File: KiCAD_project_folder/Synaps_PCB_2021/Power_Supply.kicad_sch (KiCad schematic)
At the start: 7 parts, among them J1 USB_C_Receptacle, U1 MAX14748BEWW+

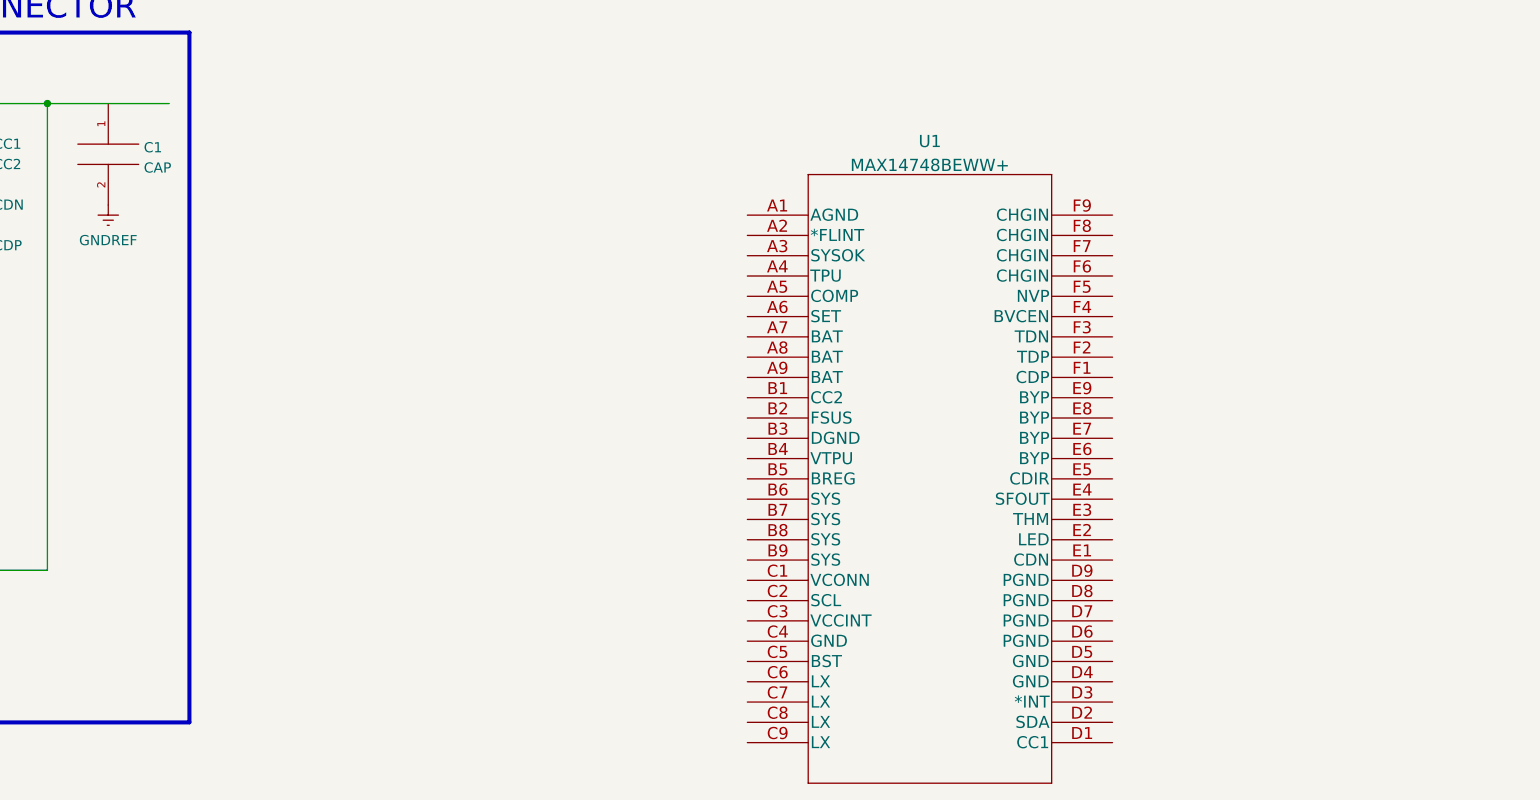
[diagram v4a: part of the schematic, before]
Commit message: modified the battery file
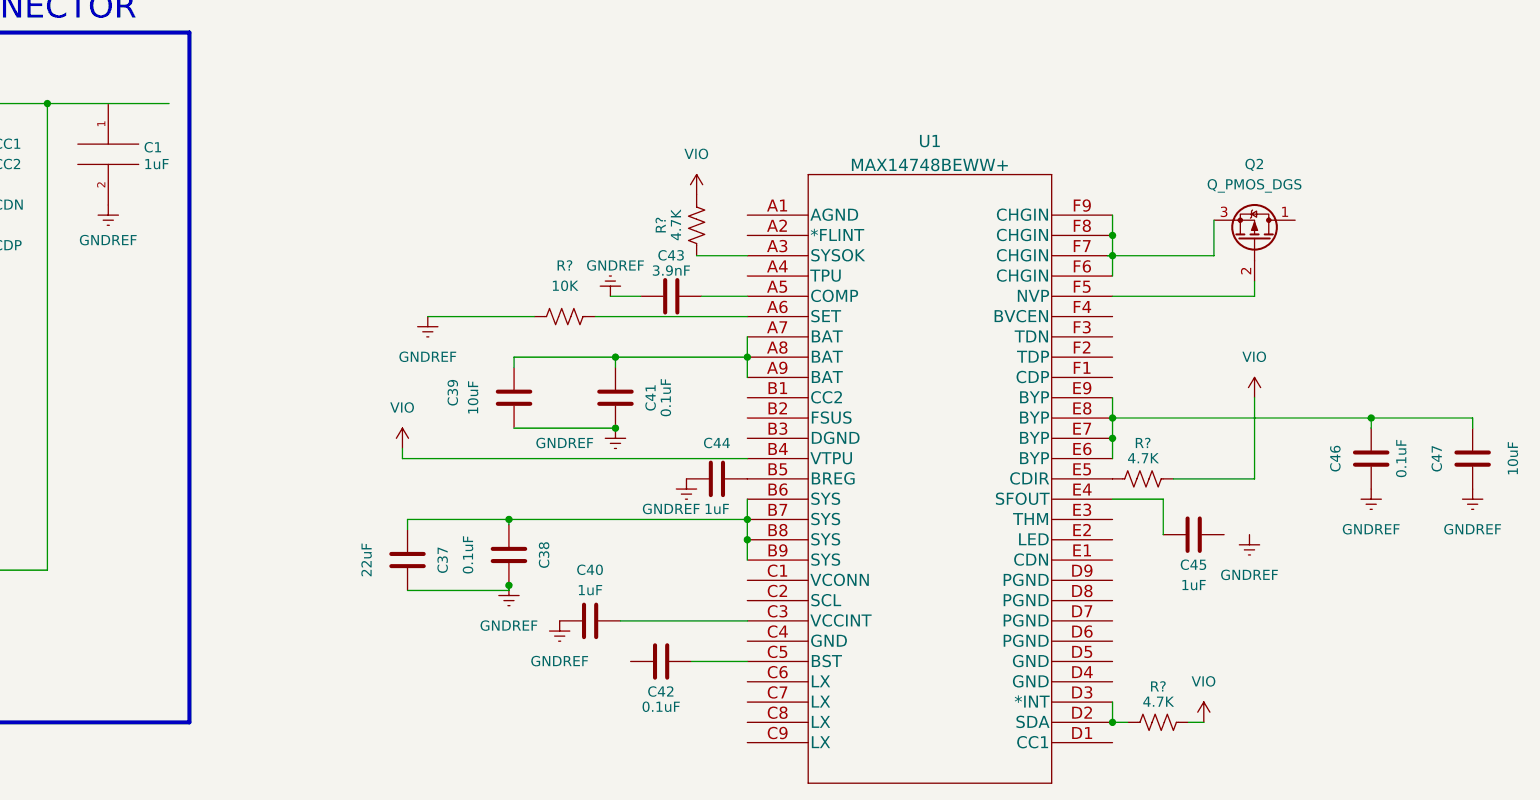
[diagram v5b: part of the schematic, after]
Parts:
- added C37: 22uF, symbol Device:C
- added C38, C41, C42, C46: 0.1uF, symbol Device:C
- added C39, C47: 10uF, symbol Device:C
- added C40, C44, C45: 1uF, symbol Device:C
- added C43: 3.9nF, symbol Device:C
- added Q2: Q_PMOS_DGS, symbol Device:Q_PMOS_DGS
- added R? (x3): 4.7K, symbol Device:R_US
- added R?: 10K, symbol Device:R_US
- C1: value CAP -> 1uF
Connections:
- net GNDREF: now also C37.2, C38.2, C39.2, C40.1, C41.2, C43.1, C44.1, C46.2, C47.2, R?.1
- net at U1.A3 (SYSOK): now also R?.1
- net at U1.A5 (COMP): now also C43.2
- net at U1.A6 (SET): now also R?.2
- net at U1.A7 (BAT): now also U1.A8 (BAT), U1.A9 (BAT), C39.1, C41.1
- net +1V1: now reaches U1.B4 (VTPU)
- net +1V1: now also R?.2, R?.2, R?.2
- net at U1.B5 (BREG): now also C44.2
- net at U1.B6 (SYS): now also U1.B7 (SYS), U1.B8 (SYS), U1.B9 (SYS), C37.1, C38.1
- net at U1.C3 (VCCINT): now also C40.2
- net at U1.C5 (BST): now also C42.2
- net at U1.D2 (SDA): now also U1.D3 (*INT), R?.1
- net at U1.E4 (SFOUT): now also C45.1
- net at U1.E5 (CDIR): now also R?.1
- net at U1.E6 (BYP): now also U1.E7 (BYP), U1.E8 (BYP), U1.E9 (BYP), C46.1, C47.1
- net at U1.F5 (NVP): now also Q2.2 (G)
- net at U1.F6 (CHGIN): now also U1.F7 (CHGIN), U1.F8 (CHGIN), U1.F9 (CHGIN), Q2.3 (S)

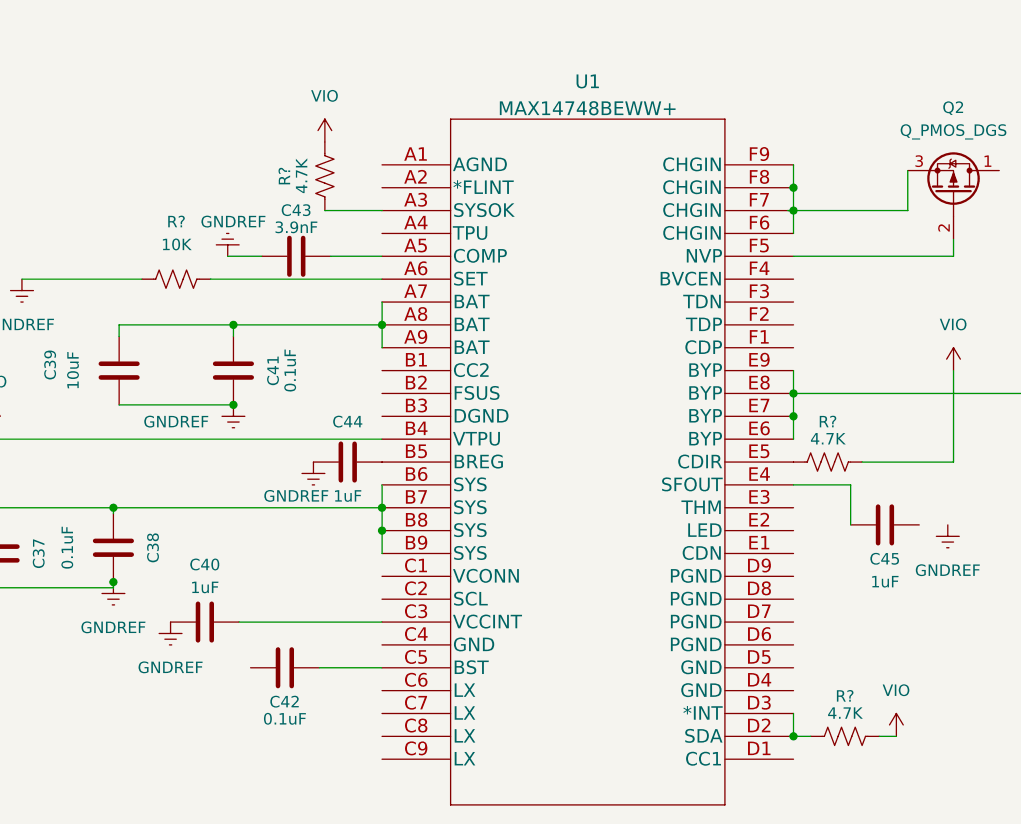
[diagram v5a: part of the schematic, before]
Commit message: Added Esp32-S2 datasheet files and hardware design guidelines to project
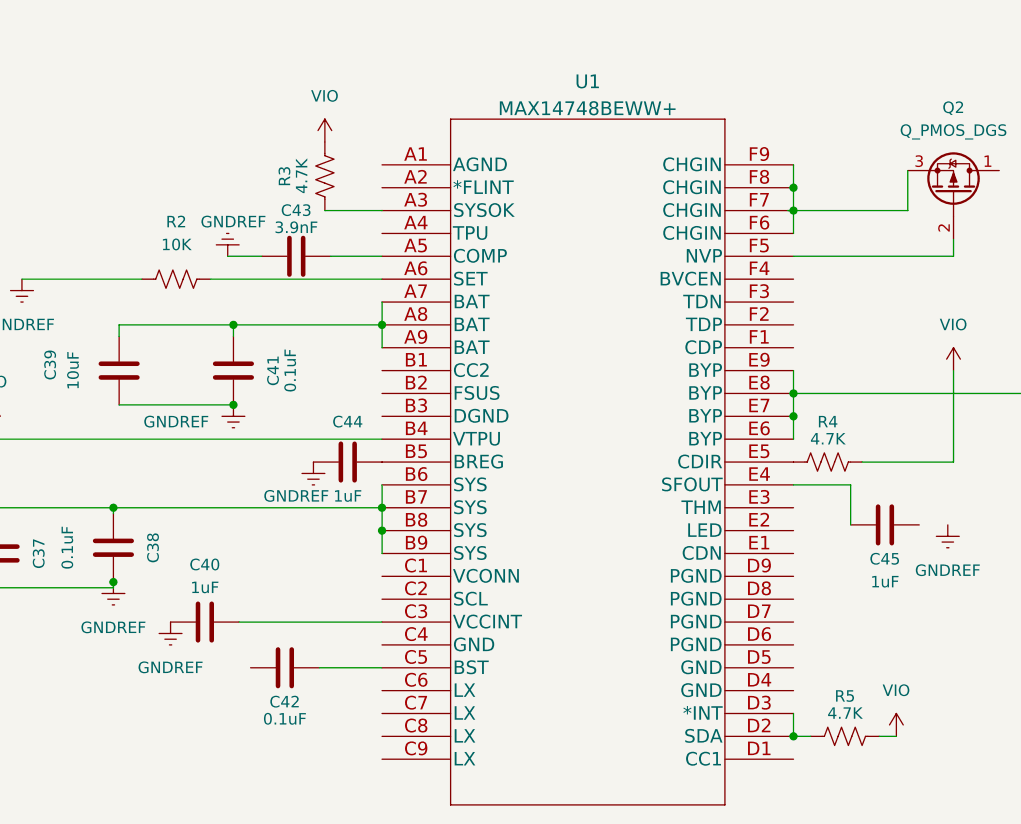
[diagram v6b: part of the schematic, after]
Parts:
- gave numbers to parts that had none: 4
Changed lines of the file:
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@@
   (symbol (lib_id "power:GNDREF") (at 157.48 76.2 0) (unit 1)
     (in_bom yes) (on_board yes)
-    (property "Reference" "#PWR?" (id 0) (at 157.48 82.55 0)
+    (property "Reference" "#PWR0104" (id 0) (at 157.48 82.55 0)
       (effects (font (size 1.27 1.27)) hide)
     )
@@
   (symbol (lib_id "project_library_MICSAPCB:VIO") (at 121.92 72.39 0) (unit 1)
     (in_bom yes) (on_board yes) (fields_autoplaced)
-    (property "Reference" "#PWR?" (id 0) (at 121.92 76.2 0)
+    (property "Reference" "#PWR0101" (id 0) (at 121.92 76.2 0)
       (effects (font (size 1.27 1.27)) hide)
     )
@@
   (symbol (lib_id "Device:R_US") (at 158.75 44.45 180) (unit 1)
     (in_bom yes) (on_board yes)
-    (property "Reference" "R?" (id 0) (at 154.305 44.45 90))
+    (property "Reference" "R3" (id 0) (at 154.305 44.45 90))
     (property "Value" "4.7K" (id 1) (at 156.21 44.45 90))
     (property "Footprint" "" (id 2) (at 157.734 44.196 90)
@@
   (symbol (lib_id "Device:R_US") (at 216.535 106.68 90) (unit 1)
     (in_bom yes) (on_board yes)
-    (property "Reference" "R?" (id 0) (at 216.535 102.235 90))
+    (property "Reference" "R5" (id 0) (at 216.535 102.235 90))
     (property "Value" "4.7K" (id 1) (at 216.535 104.14 90))
     (property "Footprint" "" (id 2) (at 216.789 105.664 90)
@@
   (symbol (lib_id "Device:R_US") (at 142.24 55.88 90) (unit 1)
     (in_bom yes) (on_board yes) (fields_autoplaced)
-    (property "Reference" "R?" (id 0) (at 142.24 49.53 90))
+    (property "Reference" "R2" (id 0) (at 142.24 49.53 90))
     (property "Value" "10K" (id 1) (at 142.24 52.07 90))
     (property "Footprint" "" (id 2) (at 142.494 54.864 90)
@@
   (symbol (lib_id "project_library_MICSAPCB:VIO") (at 158.75 40.64 0) (unit 1)
     (in_bom yes) (on_board yes) (fields_autoplaced)
-    (property "Reference" "#PWR?" (id 0) (at 158.75 44.45 0)
+    (property "Reference" "#PWR0103" (id 0) (at 158.75 44.45 0)
       (effects (font (size 1.27 1.27)) hide)
     )
@@
   (symbol (lib_id "project_library_MICSAPCB:VIO") (at 228.6 66.04 0) (unit 1)
     (in_bom yes) (on_board yes) (fields_autoplaced)
-    (property "Reference" "#PWR?" (id 0) (at 228.6 69.85 0)
+    (property "Reference" "#PWR0106" (id 0) (at 228.6 69.85 0)
       (effects (font (size 1.27 1.27)) hide)
     )
@@
   (symbol (lib_id "Device:R_US") (at 214.63 76.2 90) (unit 1)
     (in_bom yes) (on_board yes)
-    (property "Reference" "R?" (id 0) (at 214.63 71.755 90))
+    (property "Reference" "R4" (id 0) (at 214.63 71.755 90))
     (property "Value" "4.7K" (id 1) (at 214.63 73.66 90))
     (property "Footprint" "" (id 2) (at 214.884 75.184 90)
@@
   (symbol (lib_id "project_library_MICSAPCB:VIO") (at 222.25 106.68 0) (unit 1)
     (in_bom yes) (on_board yes) (fields_autoplaced)
-    (property "Reference" "#PWR?" (id 0) (at 222.25 110.49 0)
+    (property "Reference" "#PWR0105" (id 0) (at 222.25 110.49 0)
       (effects (font (size 1.27 1.27)) hide)
     )
@@
   (symbol (lib_id "power:GNDREF") (at 125.095 55.88 0) (unit 1)
     (in_bom yes) (on_board yes) (fields_autoplaced)
-    (property "Reference" "#PWR?" (id 0) (at 125.095 62.23 0)
-      (effects (font (size 1.27 1.27)) hide)
-    )
+    (property "Reference" "#PWR0102" (id 0) (at 125.095 62.23 0)
+      (effects (font (size 1.27 1.27)) hide)
+    )

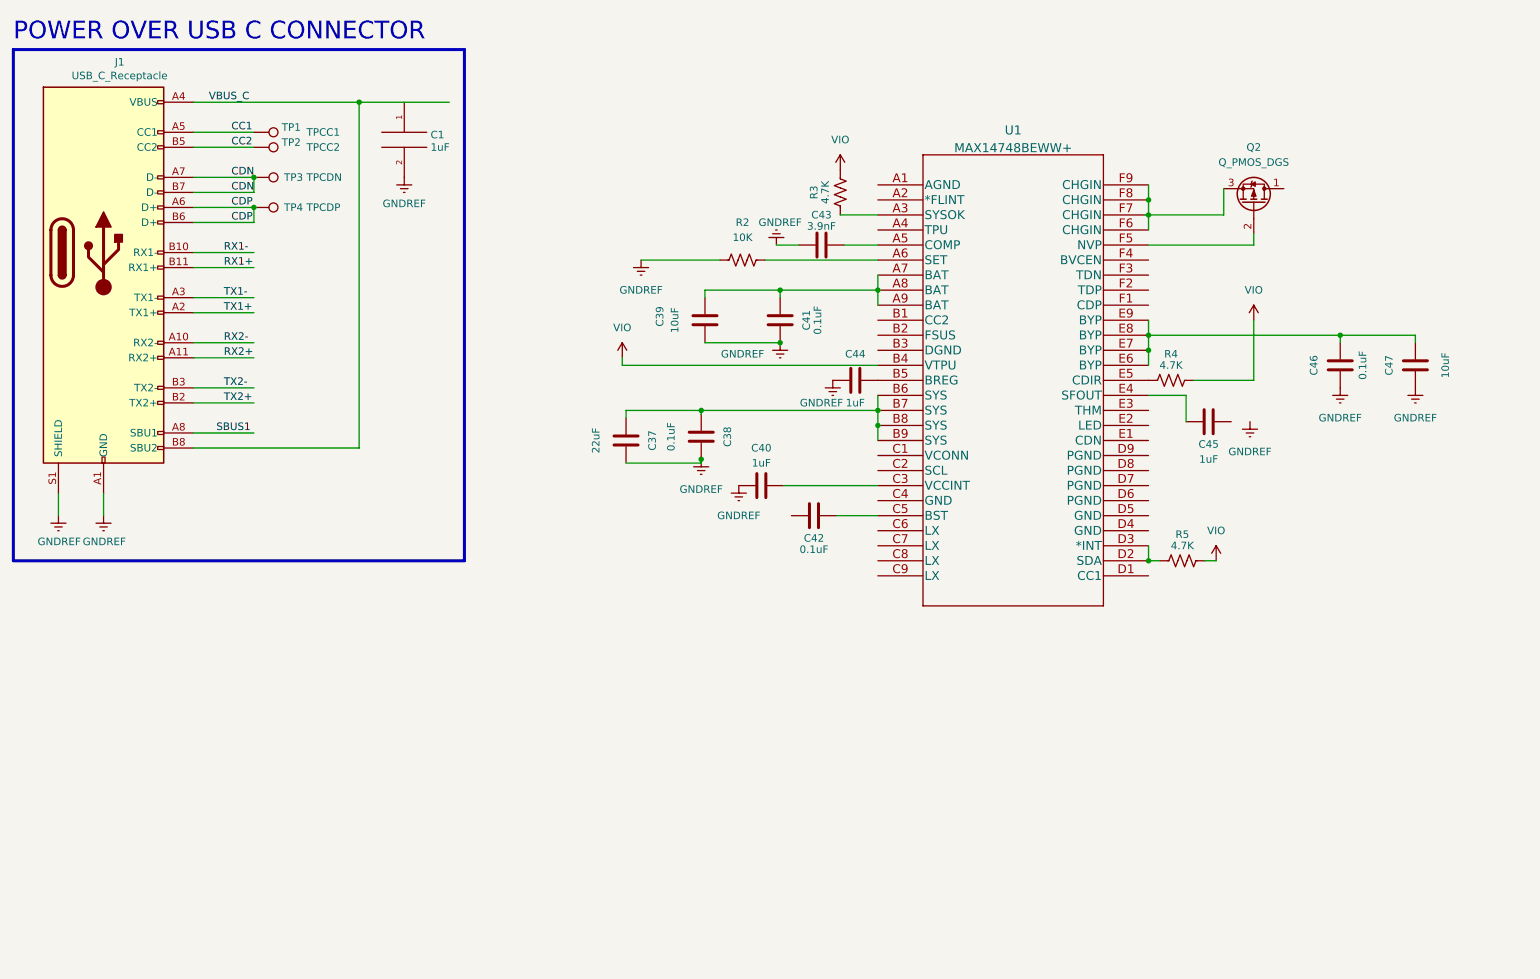
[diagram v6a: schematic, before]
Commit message: Worked on schematic for power supply
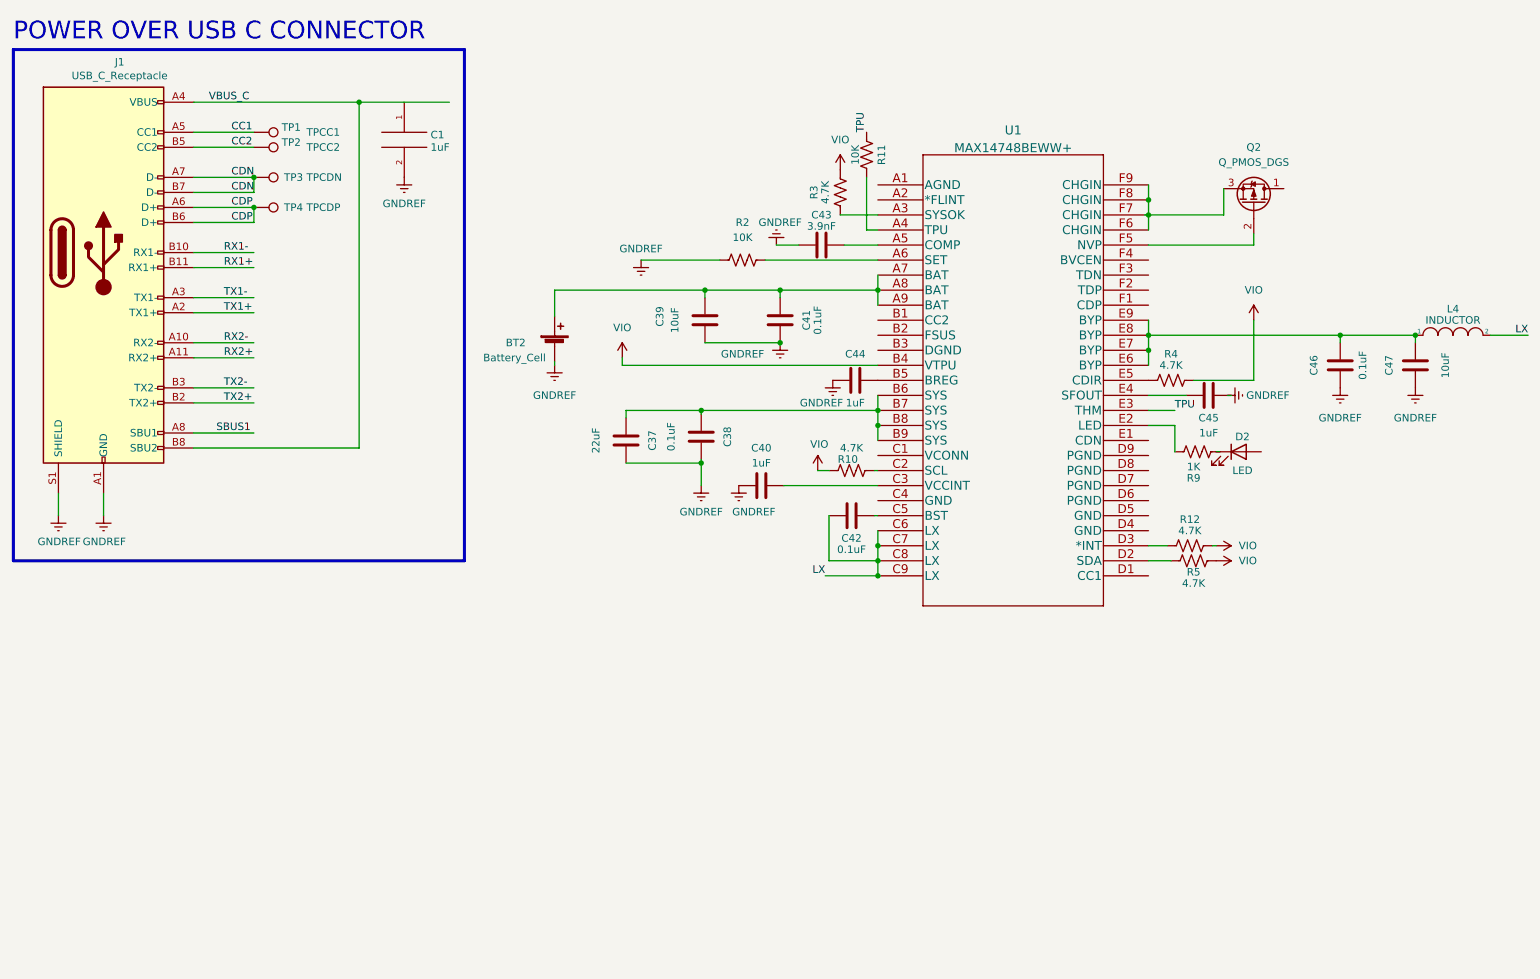
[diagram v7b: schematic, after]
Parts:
- added BT2: Battery_Cell, symbol Device:Battery_Cell
- added D2: LED, symbol Device:LED
- added L4: INDUCTOR, symbol pspice:INDUCTOR
- added R10, R12: 4.7K, symbol Device:R_US
- added R11: 10K, symbol Device:R_US
- added R9: 1K, symbol Device:R_US
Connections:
- net +1V1: now also R10.2, R12.2
- net GNDREF: now also C45.2, BT2.2 (-)
- net LX: now reaches C42.1
- net LX: now also U1.C6 (LX), U1.C7 (LX), U1.C8 (LX), U1.C9 (LX), L4.2
- net at U1.A4 (TPU): now also R11.1
- net at C39.1, C41.1, U1.A7 (BAT)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: now also BT2.1 (+)
- net at U1.C2 (SCL): now also R10.1
- net at R5.1, U1.D2 (SDA): no longer U1.D3 (*INT)
- net at U1.E2 (LED): now also R9.1
- net TPU: now reaches U1.E3 (THM)
- net TPU: now also R11.2
- net at C46.1, C47.1, U1.E6 (BYP)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: now also L4.1
- new net: R12.1, U1.D3 (*INT)
- new net: D2.1 (K), R9.2
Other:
- moved on the sheet: C42, C45, R5
